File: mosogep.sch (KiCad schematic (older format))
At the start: 74 parts

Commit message: Some progress
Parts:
- removed C? (x2): 100n, symbol Device:C
- removed C?: 1u, symbol Device:C
- removed C?: 10u, symbol Device:CP
- removed D?: bas85, symbol Device:D_Schottky
- removed J?: AC1010, symbol Connector:Conn_01x02_Male
- removed Q?: FDS9435A, Package_SO:SOIC-8_3.9x4.9mm_P1.27mm, symbol Transistor_FET:FDS9435A
- removed R? (x2): 50, symbol Device:R
- removed R? (x5): 100k, symbol Device:R
- removed R? (x3): 200k, symbol Device:R
- removed U? (x5): TL084, symbol Amplifier_Operational:TL084
- added C?: 100n, symbol Device:C
- added Q?: yjl2301c, symbol Device:Q_PMOS_GSD
- added R?: 0, symbol Device:R
- added R? (x2): R, symbol Device:R
- added U?: max1649, symbol spec_alk:max1649
- C? (x2): symbol Device:CP -> mosogep-rescue:CP-Device
- D? (x2): value D_TVS -> PGB1010603MR
- D?: value bat214 -> ss14
- FB?: symbol Device:Ferrite_Bead_Small -> mosogep-rescue:Ferrite_Bead_Small-Device
- FB?: value (none) -> HF70ACC575032-TL; symbol Device:Ferrite_Bead_Small -> mosogep-rescue:Ferrite_Bead_Small-Device
- FB?: value Ferrite_Bead_Small -> HF70ACC575032-TL; symbol Device:Ferrite_Bead_Small -> mosogep-rescue:Ferrite_Bead_Small-Device
- J?: value Conn_01x03_Male -> Programozó csati
- R? (x2): value R -> 10
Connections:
- net labels removed: AD, ADC_CSUCS_M1, ADC_DS_M, ADC_DS_M1
- wire segments 141 -> 116
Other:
- note removed: "Kell másik műveleti erősítő: pl \nMC33204DR2G\nrail-to-rail, +-3.3V-ról fog járni, nagy közös módusú elnyomás"
- note removed: "Nem lesz jó, mert negatív fesz megy így az ADC bemenetére"
- note removed: "csúcsban 2.3V"
- note removed: "csúcsban 2.3V (23A csúcsáram)"
- moved on the sheet: C?, D?, J?, L?, R?

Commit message: Improvements
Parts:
- added C?: 10n, symbol Device:C
- added D? (x2): LED, symbol Device:LED
- added R?: 33, symbol Device:R
- added R?: 10k, symbol Device:R
- added R? (x5): 330, symbol Device:R
- C?: value 10n -> 100n
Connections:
- net +3V3: now also R?.1
- net CLK_OUT: now also R?.2; no longer U?.29 (PA8)
- net GNDD: now also D?.1 (K), D?.1 (K), D?.1 (K), SW?.1, C?.2, D?.1 (K), D?.1 (K)
- net MISO: now also U?.40 (PB4); no longer U?.16 (PA6)
- net MOSI: now also U?.41 (PB5); no longer U?.17 (PA7)
- net SCLK: now also U?.39 (PB3); no longer U?.15 (PA5)
- net nCS: now also U?.42 (PB6); no longer U?.14 (PA4)
- net aram1: now reaches U?.10 (PA0)
- net aram2: now reaches U?.11 (PA1)
- net aram3: now reaches U?.12 (PA2)
- net aram4: now reaches U?.13 (PA3)
- net w5500_reset: now reaches U?.19 (PB1)
- net at U?.22 (PB11): now also R?.1
- net at U?.25 (PB12): now also R?.1
- net at U?.26 (PB13): now also R?.1
- net at U?.27 (PB14): now also R?.1
- net at U?.28 (PB15): now also R?.1
- net at U?.43 (PB7): now also SW?.2, C?.1, R?.2
- net at D?.2 (A): now also R?.2 (x3)
- new net: R?.1, U?.29 (PA8)
- new net: D?.2 (A), R?.2 (x2)
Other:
- note added: "TODO nullátmenet detektor ?"
- moved on the sheet: C?, D?, F?, FB?, J?, L?, Q?, R?, SW?, T?, U?

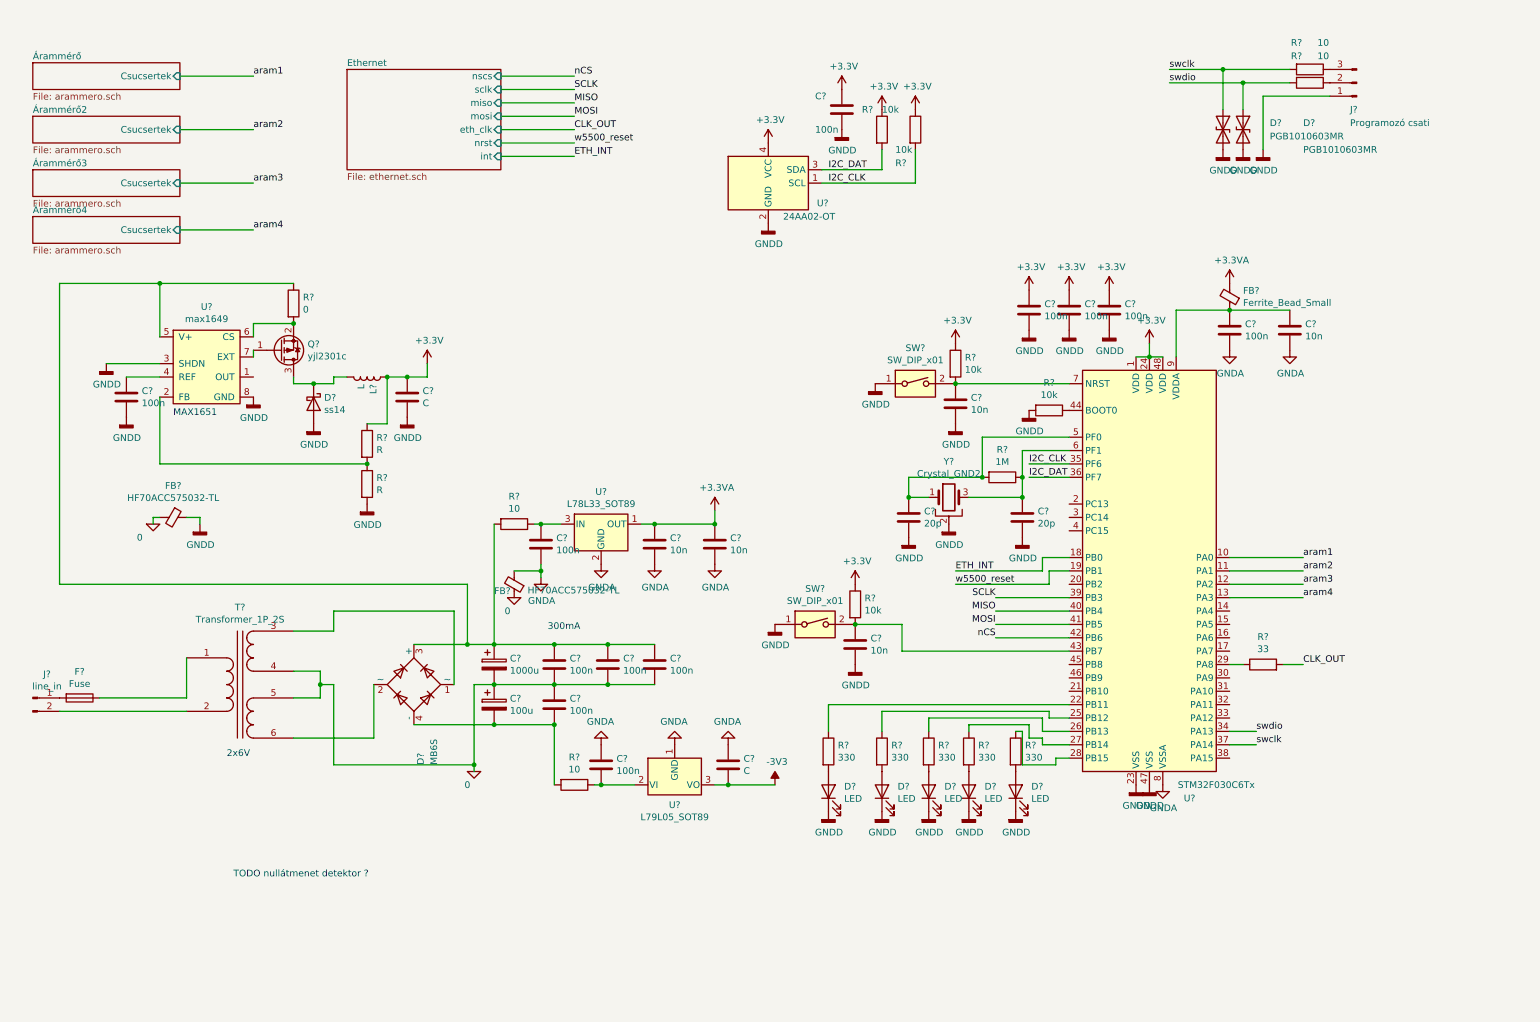
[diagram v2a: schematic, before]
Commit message: correct  op amp type to rail-to-rail
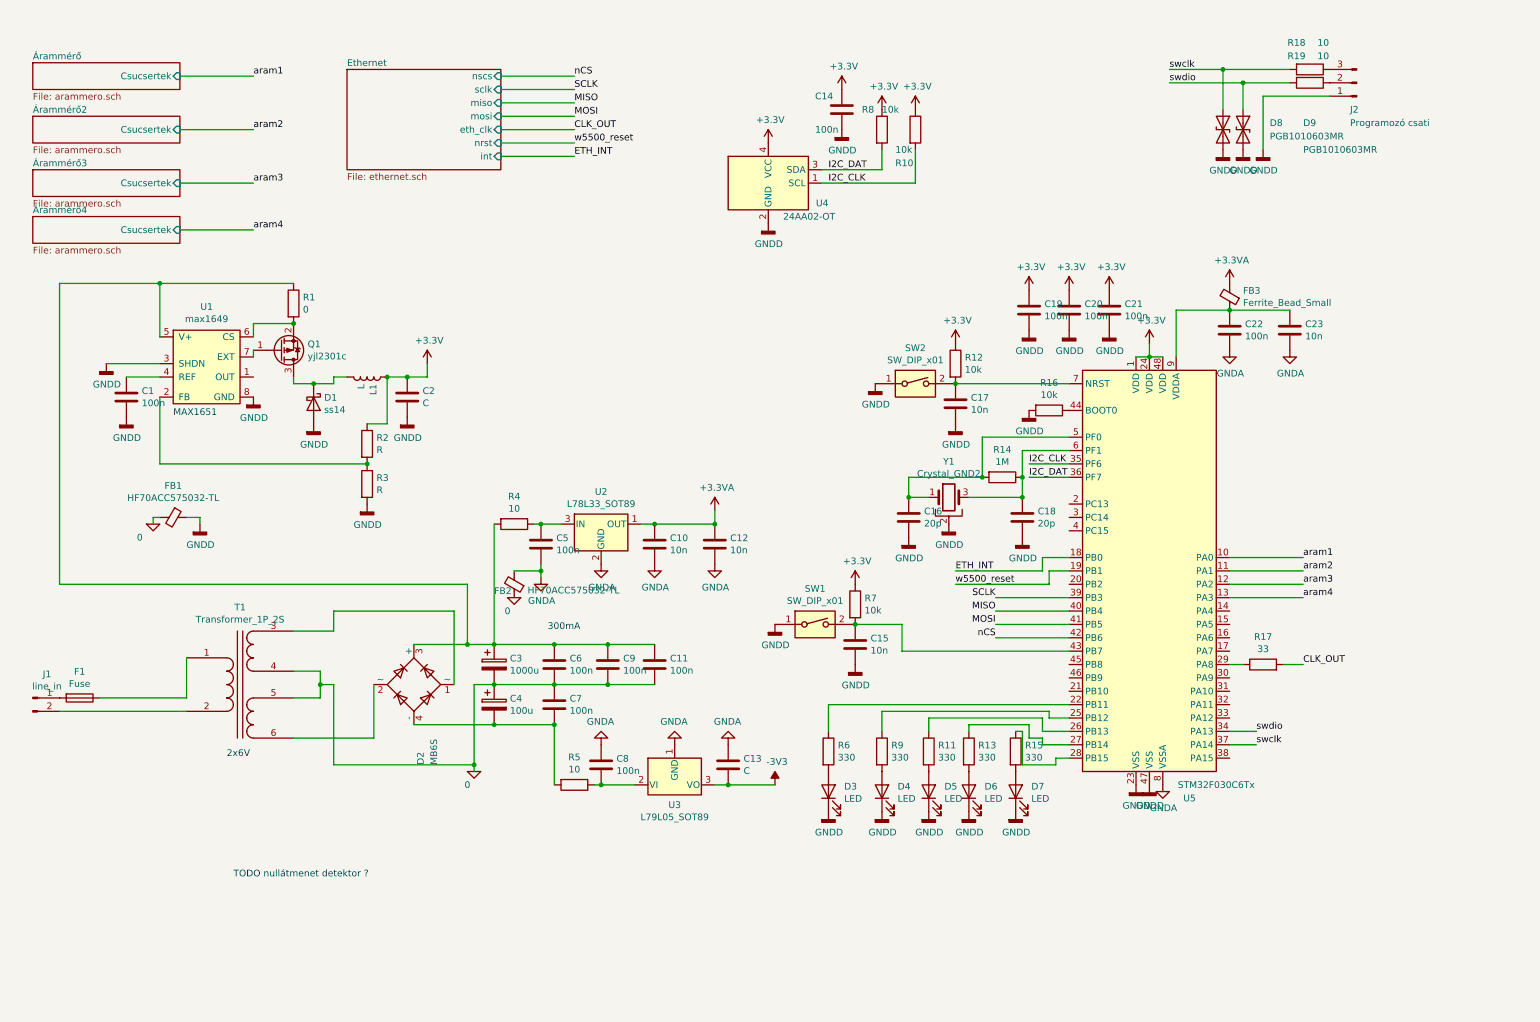
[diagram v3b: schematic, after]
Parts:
- gave numbers to parts that had none: 68

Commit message: Tápegység külön lap + fázisméréshez áramkörök
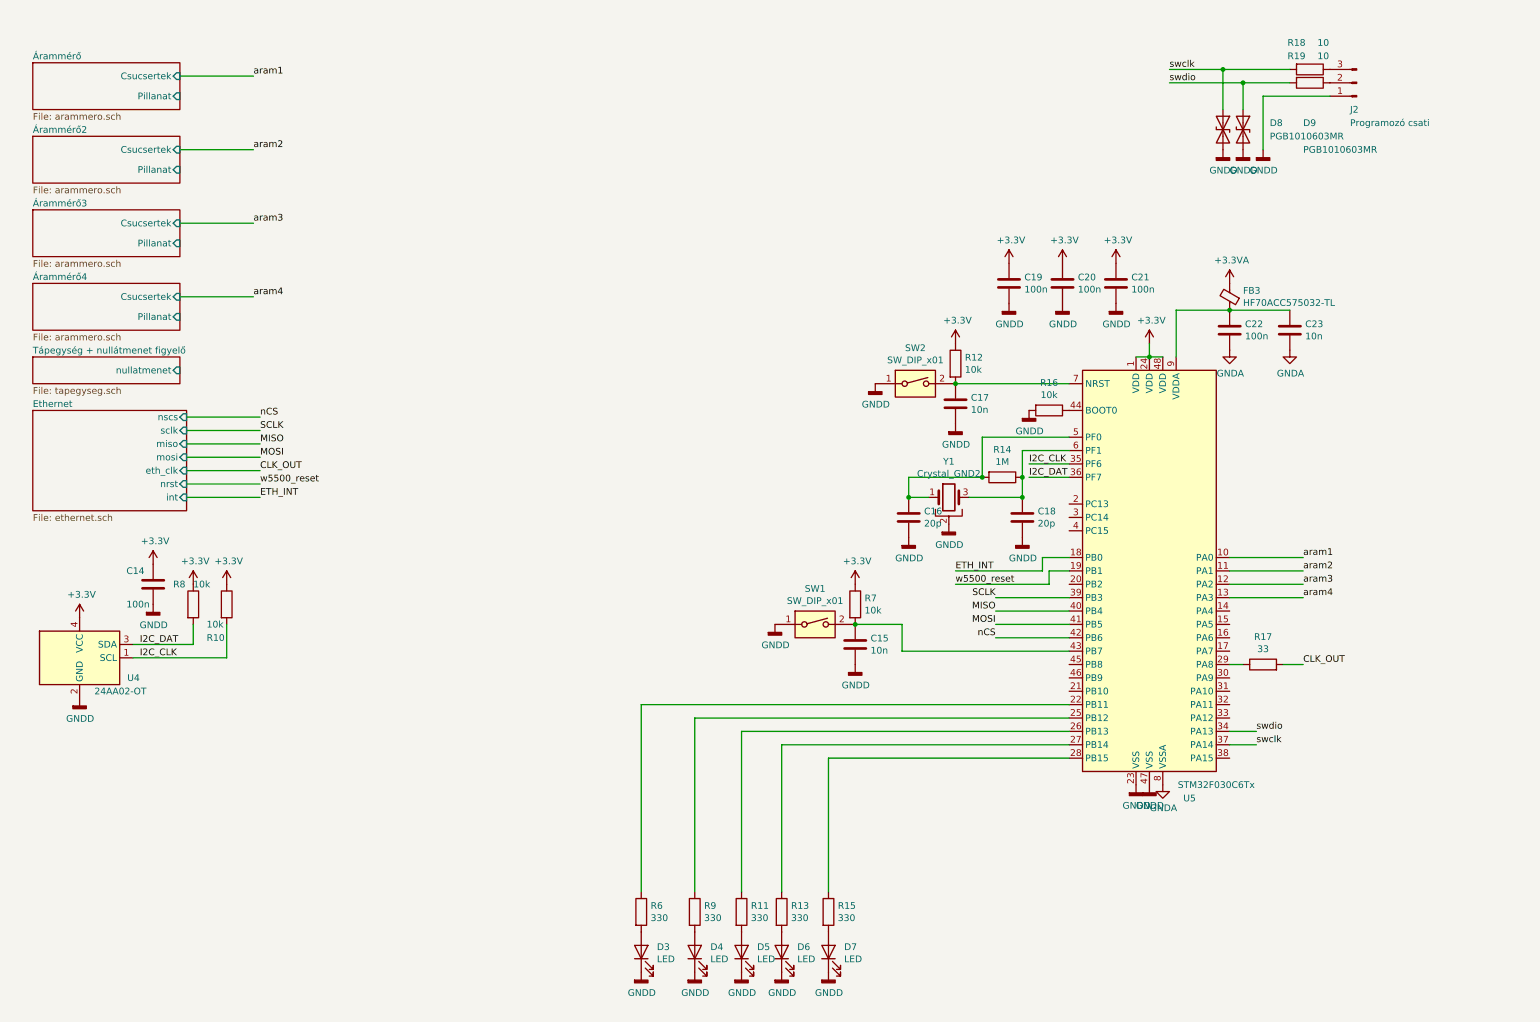
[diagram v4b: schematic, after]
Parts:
- removed C1, C11, C5, C6, C7, C8, C9: 100n, symbol Device:C
- removed C10, C12: 10n, symbol Device:C
- removed C13, C2: C, symbol Device:C
- removed C3: 1000u, symbol mosogep-rescue:CP-Device
- removed C4: 100u, symbol mosogep-rescue:CP-Device
- removed D1: ss14, symbol Device:D_Schottky
- removed D2: MB6S, Package_TO_SOT_SMD:TO-269AA, symbol Diode_Bridge:MB6S
- removed F1: Fuse, symbol Device:Fuse
- removed FB1, FB2: HF70ACC575032-TL, symbol mosogep-rescue:Ferrite_Bead_Small-Device
- removed J1: line_in, symbol Connector:Conn_01x02_Male
- removed L1: L, symbol Device:L
- removed Q1: yjl2301c, symbol Device:Q_PMOS_GSD
- removed R1: 0, symbol Device:R
- removed R2, R3: R, symbol Device:R
- removed R4, R5: 10, symbol Device:R
- removed T1: Transformer_1P_2S, symbol Device:Transformer_1P_2S
- removed U1: max1649, symbol spec_alk:max1649
- removed U2: L78L33_SOT89, Package_TO_SOT_SMD:SOT-89-3, symbol Regulator_Linear:L78L33_SOT89
- removed U3: L79L05_SOT89, Package_TO_SOT_SMD:SOT-89-3, symbol Regulator_Linear:L79L05_SOT89
- FB3: value Ferrite_Bead_Small -> HF70ACC575032-TL
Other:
- note removed: "2x6V"
- note removed: "300mA"
- note removed: "MAX1651"
- note removed: "TODO nullátmenet detektor ?"
- moved on the sheet: C14, C19, C20, C21, D3, D4, D5, D6, D7, R10, R11, R13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

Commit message: ++
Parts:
- removed R17: 33, symbol Device:R
- removed Y1: Crystal_GND2, symbol Device:Crystal_GND2
- added D6, D7: LED, LED_SMD:LED_0805_2012Metric_Pad1.15x1.40mm_HandSolder, symbol Device:LED
- added H1, H2, H3, H4: MountingHole, MountingHole:MountingHole_3mm, symbol Mechanical:MountingHole
- added R8, R9: 330, Resistor_SMD:R_0805_2012Metric_Pad1.20x1.40mm_HandSolder, symbol Device:R
- added TP23, TP24: TestPoint_2Pole, Connector_PinHeader_2.54mm:PinHeader_1x02_P2.54mm_Vertical, symbol Connector:TestPoint_2Pole
- added Y1: 8MHz, Crystal:Crystal_HC18-U_Vertical, symbol Device:Crystal
- C1: renamed from C14; footprint (none) -> Capacitor_SMD:C_0805_2012Metric_Pad1.18x1.45mm_HandSolder
- C10: renamed from C15; footprint (none) -> Capacitor_SMD:C_0805_2012Metric_Pad1.18x1.45mm_HandSolder
- C2: renamed from C16; footprint (none) -> Capacitor_SMD:C_0805_2012Metric_Pad1.18x1.45mm_HandSolder
- C3: renamed from C17; footprint (none) -> Capacitor_SMD:C_0805_2012Metric_Pad1.18x1.45mm_HandSolder
- C4: renamed from C19; footprint (none) -> Capacitor_SMD:C_0805_2012Metric_Pad1.18x1.45mm_HandSolder
- C5: renamed from C18; footprint (none) -> Capacitor_SMD:C_0805_2012Metric_Pad1.18x1.45mm_HandSolder
- C6: renamed from C20; footprint (none) -> Capacitor_SMD:C_0805_2012Metric_Pad1.18x1.45mm_HandSolder
- C7: renamed from C21; footprint (none) -> Capacitor_SMD:C_0805_2012Metric_Pad1.18x1.45mm_HandSolder
- C8: renamed from C22; footprint (none) -> Capacitor_SMD:C_0805_2012Metric_Pad1.18x1.45mm_HandSolder
- C9: renamed from C23; footprint (none) -> Capacitor_SMD:C_0805_2012Metric_Pad1.18x1.45mm_HandSolder
- D1: renamed from D3; footprint (none) -> LED_SMD:LED_0805_2012Metric_Pad1.15x1.40mm_HandSolder
- D2: renamed from D4; footprint (none) -> LED_SMD:LED_0805_2012Metric_Pad1.15x1.40mm_HandSolder
- D3: renamed from D5; footprint (none) -> LED_SMD:LED_0805_2012Metric_Pad1.15x1.40mm_HandSolder
- D4: renamed from D6; footprint (none) -> LED_SMD:LED_0805_2012Metric_Pad1.15x1.40mm_HandSolder
- D5: renamed from D7; footprint (none) -> LED_SMD:LED_0805_2012Metric_Pad1.15x1.40mm_HandSolder
- D8, D9: footprint (none) -> Diode_SMD:D_MicroMELF_Handsoldering
- FB1: renamed from FB3; footprint (none) -> Inductor_SMD:L_0805_2012Metric_Pad1.15x1.40mm_HandSolder
- J1: renamed from J2; footprint (none) -> Connector_PinSocket_2.54mm:PinSocket_1x03_P2.54mm_Vertical
- R1: renamed from R8; footprint (none) -> Resistor_SMD:R_0805_2012Metric_Pad1.20x1.40mm_HandSolder
- R10: renamed from R12; footprint (none) -> Resistor_SMD:R_0805_2012Metric_Pad1.20x1.40mm_HandSolder
- R11: renamed from R14; footprint (none) -> Resistor_SMD:R_0805_2012Metric_Pad1.20x1.40mm_HandSolder
- R12: renamed from R16; footprint (none) -> Resistor_SMD:R_0805_2012Metric_Pad1.20x1.40mm_HandSolder
- R13: renamed from R7; footprint (none) -> Resistor_SMD:R_0805_2012Metric_Pad1.20x1.40mm_HandSolder
- R14: renamed from R18; footprint (none) -> Resistor_SMD:R_0805_2012Metric_Pad1.20x1.40mm_HandSolder
- R15: renamed from R19; footprint (none) -> Resistor_SMD:R_0805_2012Metric_Pad1.20x1.40mm_HandSolder
- R2: renamed from R10; footprint (none) -> Resistor_SMD:R_0805_2012Metric_Pad1.20x1.40mm_HandSolder
- R3: renamed from R6; footprint (none) -> Resistor_SMD:R_0805_2012Metric_Pad1.20x1.40mm_HandSolder
- R4: renamed from R9; footprint (none) -> Resistor_SMD:R_0805_2012Metric_Pad1.20x1.40mm_HandSolder
- R5: renamed from R11; footprint (none) -> Resistor_SMD:R_0805_2012Metric_Pad1.20x1.40mm_HandSolder
- R6: renamed from R13; footprint (none) -> Resistor_SMD:R_0805_2012Metric_Pad1.20x1.40mm_HandSolder
- R7: renamed from R15; footprint (none) -> Resistor_SMD:R_0805_2012Metric_Pad1.20x1.40mm_HandSolder
- SW1: renamed from SW2; footprint (none) -> Button_Switch_THT:SW_TH_Tactile_Omron_B3F-10xx
- SW2: renamed from SW1; footprint (none) -> Button_Switch_THT:SW_TH_Tactile_Omron_B3F-10xx
- renumbered U4 to U1, U5 to U2
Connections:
- net ETH_INT: now also U2.20 (PB2); no longer U2.18 (PB0)
- net GNDA: now also TP23.1, TP23.2
- net GNDD: now also D6.1 (K), D7.1 (K), TP24.1, TP24.2
- net I2C_CLK: now also U2.21 (PB10); no longer U2.35 (PF6)
- net I2C_DAT: now also U2.22 (PB11); no longer U2.36 (PF7)
- net MISO: now also U2.27 (PB14); no longer U2.40 (PB4)
- net MOSI: now also U2.28 (PB15); no longer U2.41 (PB5)
- net SCLK: now also U2.26 (PB13); no longer U2.39 (PB3)
- net aram2: now also U2.12 (PA2); no longer U2.11 (PA1)
- net aram3: now also U2.11 (PA1); no longer U2.12 (PA2)
- net nCS: now also U2.25 (PB12); no longer U2.42 (PB6)
- net at R3.1: now also U2.39 (PB3); no longer U2.22 (PB11)
- net at R4.1: now also U2.40 (PB4); no longer U2.25 (PB12)
- net at R5.1: now also U2.41 (PB5); no longer U2.26 (PB13)
- net at R6.1: now also U2.42 (PB6); no longer U2.27 (PB14)
- net at R7.1: now also U2.43 (PB7); no longer U2.28 (PB15)
- net fazisdetektor4: now reaches U2.29 (PA8)
- net fazisdetektor3: now reaches U2.30 (PA9)
- net fazisdetektor2: now reaches U2.31 (PA10)
- net fazisdetektor1: now reaches U2.32 (PA11)
- net fazis_referencia: now reaches U2.33 (PA12)
- net at U2.38 (PA15): now also C10.1, R13.2, SW2.2
- net at U2.45 (PB8): now also R8.1
- net at U2.46 (PB9): now also R9.1
- net at C2.1, R11.2, U2.5 (PF0): now also Y1.1
- net at C5.1, R11.1, U2.6 (PF1): now also Y1.2
- new net: D6.2 (A), R8.2
- new net: D7.2 (A), R9.2
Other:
- moved on the sheet: C10, C2, C3, C4, C5, C6, C7, C8, C9, D1, D2, D3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
